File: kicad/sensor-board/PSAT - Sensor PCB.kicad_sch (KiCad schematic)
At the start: 36 parts, among them J1 Conn_01x06, J2 Conn_01x02, J3 Conn_01x03_Pin, J4 Conn_01x03, J6 MCU - Conn_01x04, Q1 Q_NPN_BCE, U1 MPU-6000, U2 BME280, U3 ADXL375, U4 CD-PA1616D, U5 ESP32-CAM

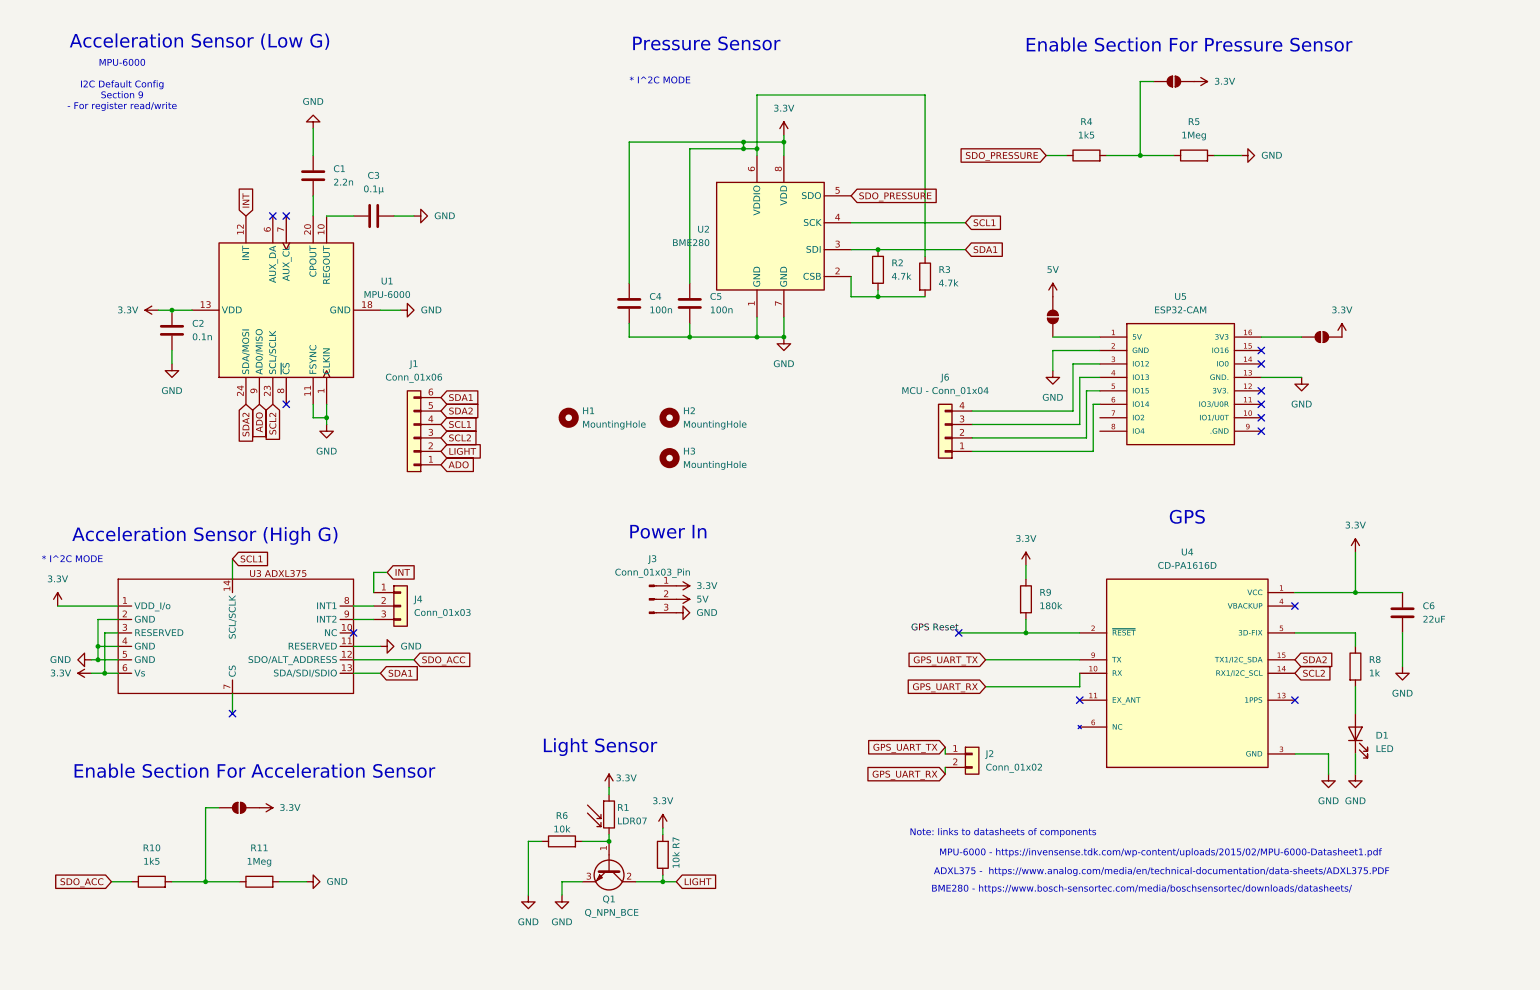
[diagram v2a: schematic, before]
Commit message: feat: new sensor board pcb & schematic (after feedback)
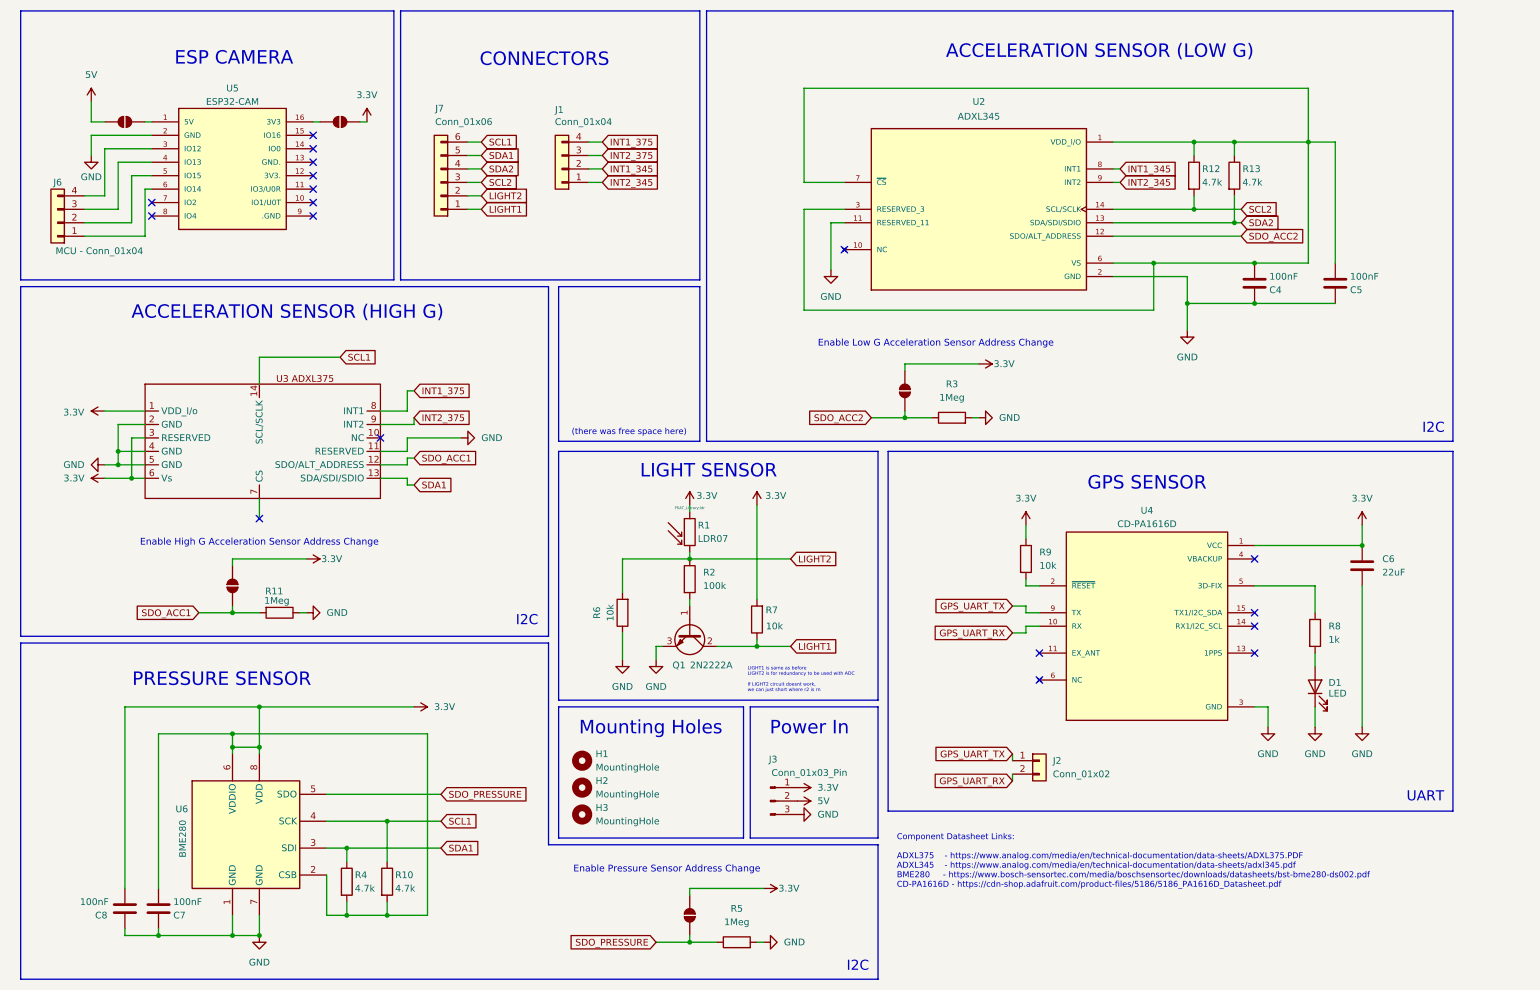
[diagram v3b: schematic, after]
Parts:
- removed C1: 2.2n, Capacitor_SMD:C_0805_2012Metric_Pad1.18x1.45mm_HandSolder, symbol Device:C
- removed C2: 0.1n, Capacitor_SMD:C_0805_2012Metric_Pad1.18x1.45mm_HandSolder, symbol Device:C
- removed C3: 0.1μ, Capacitor_SMD:C_0805_2012Metric_Pad1.18x1.45mm_HandSolder, symbol Device:C
- removed J1: Conn_01x06, Connector_PinHeader_2.54mm:PinHeader_1x06_P2.54mm_Vertical, symbol Connector_Generic:Conn_01x06
- removed J4: Conn_01x03, Connector_PinHeader_2.54mm:PinHeader_1x03_P2.54mm_Vertical, symbol Connector_Generic:Conn_01x03
- removed U1: MPU-6000, mpu6000:QFN-24-EP, symbol Sensor_Motion:MPU-6000
- removed U2: BME280, bme280:PSON65P250X250X100-8N, symbol Sensor:BME280
- added C7, C8: 100nF, Capacitor_SMD:C_0805_2012Metric_Pad1.18x1.45mm_HandSolder, symbol Device:C
- added J1: Conn_01x04, Connector_PinHeader_2.54mm:PinHeader_1x04_P2.54mm_Vertical, symbol Connector_Generic:Conn_01x04
- added J7: Conn_01x06, Connector_PinHeader_2.54mm:PinHeader_1x06_P2.54mm_Vertical, symbol Connector_Generic:Conn_01x06
- added JP5: EN_5, Jumper:SolderJumper-2_P1.3mm_Open_Pad1.0x1.5mm, symbol Jumper:SolderJumper_2_Open
- added R12, R13: 4.7k, Resistor_SMD:R_0805_2012Metric_Pad1.20x1.40mm_HandSolder, symbol Device:R
- added U2: ADXL345, ADXL345:adxl345, symbol adxl345:ADXL345
- added U6: BME280, bme280:PSON65P250X250X100-8N, symbol Sensor:BME280
- C4, C5: value 100n -> 100nF
- Q1: value Q_NPN_BCE -> 2N2222A
- R1: footprint OptoDevice:R_LDR_D13.8mm_P9.0mm_Vertical -> PSAT_Library:ldr
- R10, R4: value 1k5 -> 4.7k
- R2: value 4.7k -> 100k
- R3: value 4.7k -> 1Meg
- R9: value 180k -> 10k
- U3: footprint ADXL375:PQFN80P500X300X100-14N -> ADXL375:adxl375
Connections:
- net 3.3V: now also R10.2, R4.2, C7.1, C8.2, JP5.1 (A), U6.2 (CSB), U6.6 (VDDIO), U6.8 (VDD); no longer C4.1, C5.1, R3.1
- net GND: now also R11.1, R3.2, C7.2, C8.1, U2.11 (RESERVED_11), U2.2 (GND), U2.4 (GND), U2.5 (GND), U6.1 (GND), U6.7 (GND); no longer R11.2, U5.13 (GND.)
- net SCL1: now also R10.1, J7.6 (Pin_6), U6.4 (SCK)
- net SCL2: now also J7.3 (Pin_3), R12.2, U2.14 (SCL/SCLK); no longer U4.14 (RX1/I2C_SCL)
- net SDA1: now also R4.1, J7.5 (Pin_5), U6.3 (SDI); no longer R2.1
- net SDA2: now also J7.4 (Pin_4), R13.2, U2.13 (SDA/SDI/SDIO); no longer U4.15 (TX1/I2C_SDA)
- net SDO_PRESSURE: now also R5.1, JP5.2 (B), U6.5 (SDO); no longer R4.1
- net INT1_375: now reaches U3.8 (INT1)
- net INT1_375: now also J1.4 (Pin_4)
- net INT2_375: now reaches U3.9 (INT2)
- net INT2_375: now also J1.3 (Pin_3)
- net LIGHT2: now reaches R1.2, R6.2
- net LIGHT2: now also R2.1, J7.2 (Pin_2); no longer Q1.1 (B)
- net at R2.2: now also Q1.1 (B); no longer R3.2
- net GPS Reset: no longer names the net of R9.2, U4.2 (~{RESET})
- net LIGHT renamed LIGHT1
- net LIGHT1: now also J7.1 (Pin_1)
- net SDO_ACC renamed SDO_ACC1
- net SDO_ACC1: now also JP2.2 (B), R11.2; no longer R10.1
- new net: C4.1, C5.1, R12.1, R13.1, U2.1 (VDD_I/O), U2.3 (RESERVED_3), U2.6 (VS), U2.7 (~{CS})
- new net INT1_345: J1.2 (Pin_2), U2.8 (INT1)
- new net INT2_345: J1.1 (Pin_1), U2.9 (INT2)
- new net SDO_ACC2: JP1.2 (B), R3.1, U2.12 (SDO/ALT_ADDRESS)
- no-connect marks 15 -> 18
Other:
- note added: "(there was free space here)"
- note added: "ACCELERATION SENSOR (HIGH G)"
- note added: "ACCELERATION SENSOR (LOW G)"
- note added: "CONNECTORS"
- note added: "Component Datasheet Links: ADXL375 - https://www.analog.com/media/en/technical-documentation/data-sheets/ADXL375.PDF ADXL345 - https://www.analog.com/media/en/technical-documentation/data-sheets/adxl345.pdf BME280 - https://www.bosch-sensortec.com/media/boschsensortec/downloads/datasheets/bst-bme280-ds002.pdf CD-PA1616D - https://cdn-shop.adafruit.com/product-files/5186/5186_PA1616D_Datasheet.pdf"
- note added: "ESP CAMERA"
- note added: "Enable High G Acceleration Sensor Address Change"
- note added: "Enable Low G Acceleration Sensor Address Change"
- note added: "Enable Pressure Sensor Address Change"
- note added: "GPS SENSOR"
- note added: "I2C"
- note added: "LIGHT SENSOR"
- note added: "LIGHT1 is same as before LIGHT2 is for redundancy to be used with ADC If LIGHT2 circuit doesnt work, we can just short where r2 is rn"
- note added: "Mounting Holes"
- note added: "PRESSURE SENSOR"
- note added: "UART"
- note removed: "* I^2C MODE"
- note removed: "ADXL375 - https://www.analog.com/media/en/technical-documentation/data-sheets/ADXL375.PDF"
- note removed: "Acceleration Sensor (High G)"
- note removed: "Acceleration Sensor (Low G)"
- note removed: "BME280 - https://www.bosch-sensortec.com/media/boschsensortec/downloads/datasheets/"
- note removed: "Enable Section For Acceleration Sensor"
- note removed: "Enable Section For Pressure Sensor"
- note removed: "GPS"
- note removed: "Light Sensor"
- note removed: "MPU-6000 - https://invensense.tdk.com/wp-content/uploads/2015/02/MPU-6000-Datasheet1.pdf"
- note removed: "MPU-6000 I2C Default Config Section 9 - For register read/write"
- note removed: "Note: links to datasheets of components"
- note removed: "Pressure Sensor"
- title: Acceleration (Low/High G), Pressure, Light and GPS Sensors -> Pressure, Light, Acceleration and GPS Sensors
- moved on the sheet: C6, D1, H1, H2, H3, J2, J3, J6, Q1, R1, R11, R5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

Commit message: feat: Added Test points to the sensor PCB, swapped headers for 4pin picoclasps. fix: added decoupling and connected power for sensors
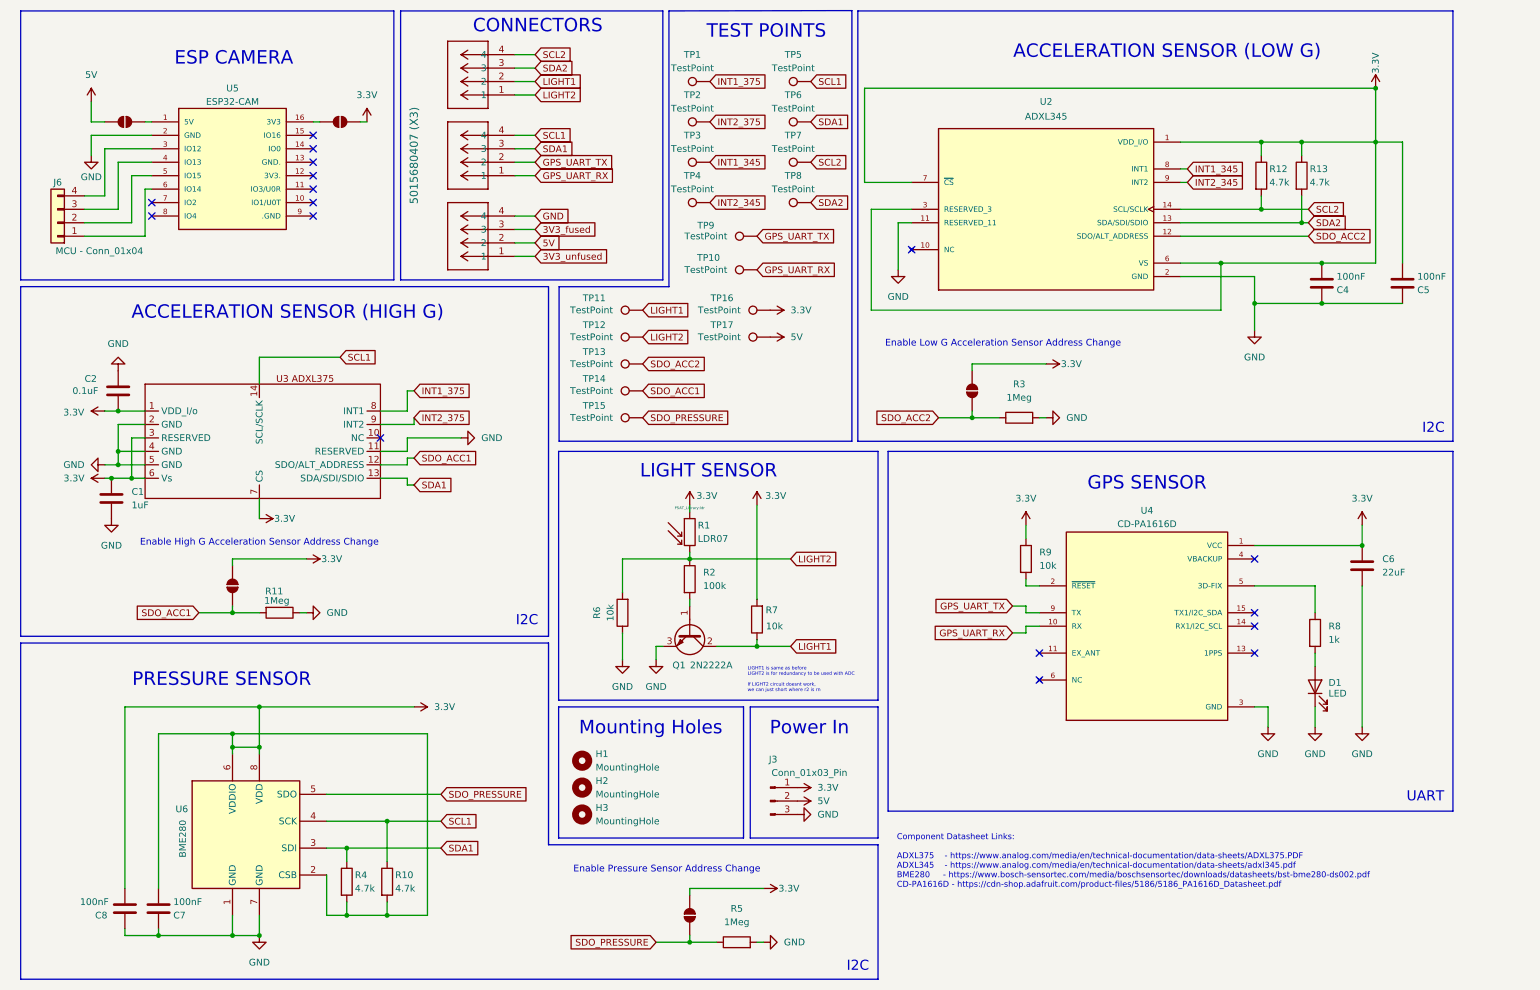
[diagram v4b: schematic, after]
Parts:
- removed J1: Conn_01x04, Connector_PinHeader_2.54mm:PinHeader_1x04_P2.54mm_Vertical, symbol Connector_Generic:Conn_01x04
- removed J2: Conn_01x02, Connector_PinHeader_2.54mm:PinHeader_1x02_P2.54mm_Vertical, symbol Connector_Generic:Conn_01x02
- removed J7: Conn_01x06, Connector_PinHeader_2.54mm:PinHeader_1x06_P2.54mm_Vertical, symbol Connector_Generic:Conn_01x06
- added C1: 1uF, symbol Device:C
- added C2: 0.1uF, symbol Device:C
- added J1, J5: 5015680407, footprints:CONN_5015680000-SD_04_MOL, symbol 2026-01-26_05-30-52:5015680407
- added J4: 5015680407 (X3), footprints:CONN_5015680000-SD_04_MOL, symbol 2026-01-26_05-30-52:5015680407
- added TP1, TP10, TP11, TP12, TP13, TP14, TP15, TP16, TP17, TP2, TP3, TP4, TP5, TP6, TP7, TP8, TP9: TestPoint, symbol Connector:TestPoint
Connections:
- net 3.3V: now also C4.1, C5.1, R12.1, R13.1, U2.1 (VDD_I/O), U2.3 (RESERVED_3), U2.6 (VS), U2.7 (~{CS}), U3.7 (CS), C1.1, C2.2, TP16.1
- net 5V: now also J1.2, TP17.1
- net GND: now also C1.2, C2.1, J1.4
- net GPS_UART_RX: now also J4.1, TP10.1
- net GPS_UART_TX: now also J4.2, TP9.1
- net INT1_345: now also TP3.1
- net INT1_375: now also TP1.1
- net INT2_345: now also TP4.1
- net INT2_375: now also TP2.1
- net LIGHT1: now also J5.2, TP11.1
- net LIGHT2: now also J5.1, TP12.1
- net SCL1: now also J4.4, TP5.1
- net SCL2: now also J5.4, TP7.1
- net SDA1: now also J4.3, TP6.1
- net SDA2: now also J5.3, TP8.1
- net SDO_ACC1: now also TP14.1
- net SDO_ACC2: now also TP13.1
- net SDO_PRESSURE: now also TP15.1
- new net 3V3_fused: J1.3
- new net 3V3_unfused: J1.1
- no-connect marks 18 -> 17
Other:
- note added: "TEST POINTS"
- note removed: "(there was free space here)"
- moved on the sheet: C4, C5, R12, R13, R3, U2

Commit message: feat: Fixed SDO label & confirmed validity of layout
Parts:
- C4: value 100nF -> 1uF
- C5: value 100nF -> 0.1uF
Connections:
- net SDO_PRESSURE: no longer JP5.2 (B), R5.1, U6.5 (SDO)
- new net PRESSURE_ADDR: JP5.2 (B), R5.1, U6.5 (SDO)
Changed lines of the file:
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@@
 	(wire
 		(pts
-			(xy 74.93 171.45) (xy 92.71 171.45)
+			(xy 74.93 171.45) (xy 100.33 171.45)
 		)
 		(stroke
@@
 		)
 	)
-	(global_label "SDO_PRESSURE"
-		(shape input)
-		(at 133.35 189.23 180)
-		(fields_autoplaced yes)
-		(effects
-			(font
-				(size 1.27 1.27)
-			)
-			(justify right)
-		)
-		(property "Intersheetrefs" "${INTERSHEET_REFS}"
-			(at 115.7297 189.23 0)
-			(effects
-				(font
-					(size 1.27 1.27)
-				)
-				(justify right)
-				(hide yes)
-			)
-		)
-	)
 	(global_label "INT1_345"
 		(shape input)
@@
 		)
 	)
-	(global_label "SDO_PRESSURE"
+	(global_label "PRESSURE_ADDR"
 		(shape input)
 		(at 92.71 161.29 0)
@@
 		)
 		(property "Intersheetrefs" "${INTERSHEET_REFS}"
-			(at 110.3303 161.29 0)
+			(at 111.4189 161.29 0)
 			(effects
 				(font
@@
 	(global_label "SDA1"
 		(shape input)
-		(at 92.71 171.45 0)
+		(at 100.33 171.45 0)
 		(fields_autoplaced yes)
 		(effects
@@
 		)
 		(property "Intersheetrefs" "${INTERSHEET_REFS}"
-			(at 99.2633 171.45 0)
+			(at 106.8833 171.45 0)
 			(effects
 				(font
@@
 		)
 	)
+	(global_label "PRESSURE_ADDR"
+		(shape input)
+		(at 133.35 189.23 180)
+		(fields_autoplaced yes)
+		(effects
+			(font
+				(size 1.27 1.27)
+			)
+			(justify right)
+		)
+		(property "Intersheetrefs" "${INTERSHEET_REFS}"
+			(at 114.6411 189.23 0)
+			(effects
+				(font
+					(size 1.27 1.27)
+				)
+				(justify right)
+				(hide yes)
+			)
+		)
+	)
 	(global_label "GPS_UART_TX"
 		(shape input)
@@
 			)
 		)
-		(property "Value" "100nF"
+		(property "Value" "1uF"
 			(at 261.874 63.5 0)
 			(effects
@@
 			)
 		)
-		(property "Value" "100nF"
+		(property "Value" "0.1uF"
 			(at 277.114 63.5 0)
 			(effects
